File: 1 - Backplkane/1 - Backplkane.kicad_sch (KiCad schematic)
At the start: 37 parts, among them J1 BUS 1, J10 EXTENDED BUS, J11 5V DC, J2 BUS 2, J3 BUS 3, J4 BUS 4, J5 BUS 5, J6 BUS 6, J7 BUS 7, J8 BUS 8, J9 BASIC BUS, U1 LD1117AV33

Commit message: Converted files from version 6 to 7 of KiCad
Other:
- company: Frederic Segard - aka: The Micro Hobbyist -> Frederic Segard
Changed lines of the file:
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@@
   (title_block
     (title "8-slot ISA-style backblane with breadboard connectivity")
-    (date "2022-10-12")
-    (rev "1.5")
-    (company "Frederic Segard - aka: The Micro Hobbyist")
+    (date "2023-08-22")
+    (rev "1.1")
+    (company "Frederic Segard")
+    (comment 1 "@microhobbyist")
   )
   (junction (at 180.34 152.4) (diameter 0) (color 0 0 0 0)
@@
     )
   )
-  (symbol (lib_id "Graphic:Logo_Open_Hardware_Small") (at 258.445 180.34 0) (unit 1)
-    (in_bom no) (on_board no) (dnp no) (fields_autoplaced)
-    (property "Reference" "#LOGO1" (at 258.445 173.355 0)
+  (symbol (lib_id "Graphic:Logo_Open_Hardware_Small") (at 259.08 180.34 0) (unit 1)
+    (in_bom no) (on_board yes) (dnp no) (fields_autoplaced)
+    (property "Reference" "#LOGO1" (at 259.08 173.355 0)
       (effects (font (size 1.27 1.27)) hide)
     )
-    (property "Value" "Logo_Open_Hardware_Small" (at 258.445 186.055 0)
+    (property "Value" "Logo_Open_Hardware_Small" (at 259.08 186.055 0)
       (effects (font (size 1.27 1.27)) hide)
     )
-    (property "Footprint" "Symbol:OSHW-Logo2_9.8x8mm_SilkScreen" (at 258.445 180.34 0)
+    (property "Footprint" "Symbol:OSHW-Logo2_9.8x8mm_SilkScreen" (at 259.08 180.34 0)
       (effects (font (size 1.27 1.27)) hide)
     )
-    (property "Datasheet" "~" (at 258.445 180.34 0)
+    (property "Datasheet" "~" (at 259.08 180.34 0)
       (effects (font (size 1.27 1.27)) hide)
     )
-    (property "Sim.Enable" "0" (at 258.445 180.34 0)
+    (property "Sim.Enable" "0" (at 259.08 180.34 0)
       (effects (font (size 1.27 1.27)) hide)
     )

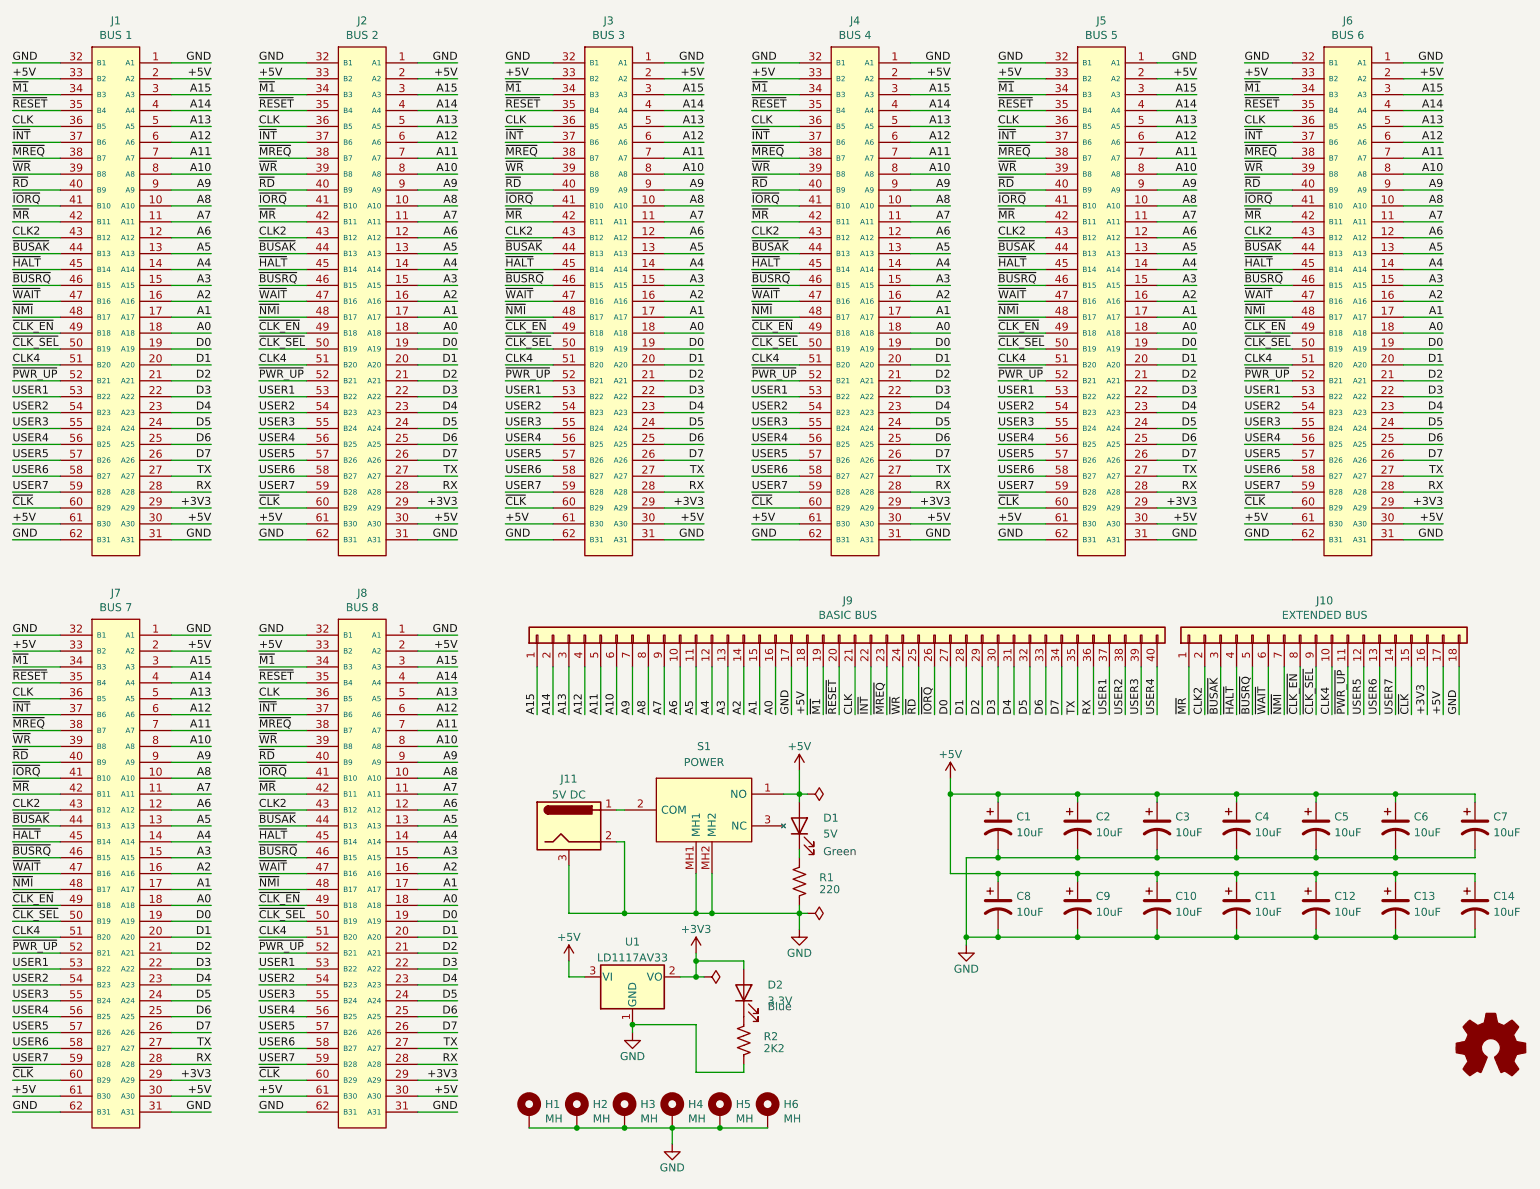
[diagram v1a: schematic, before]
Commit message: Added serial card, still needs work
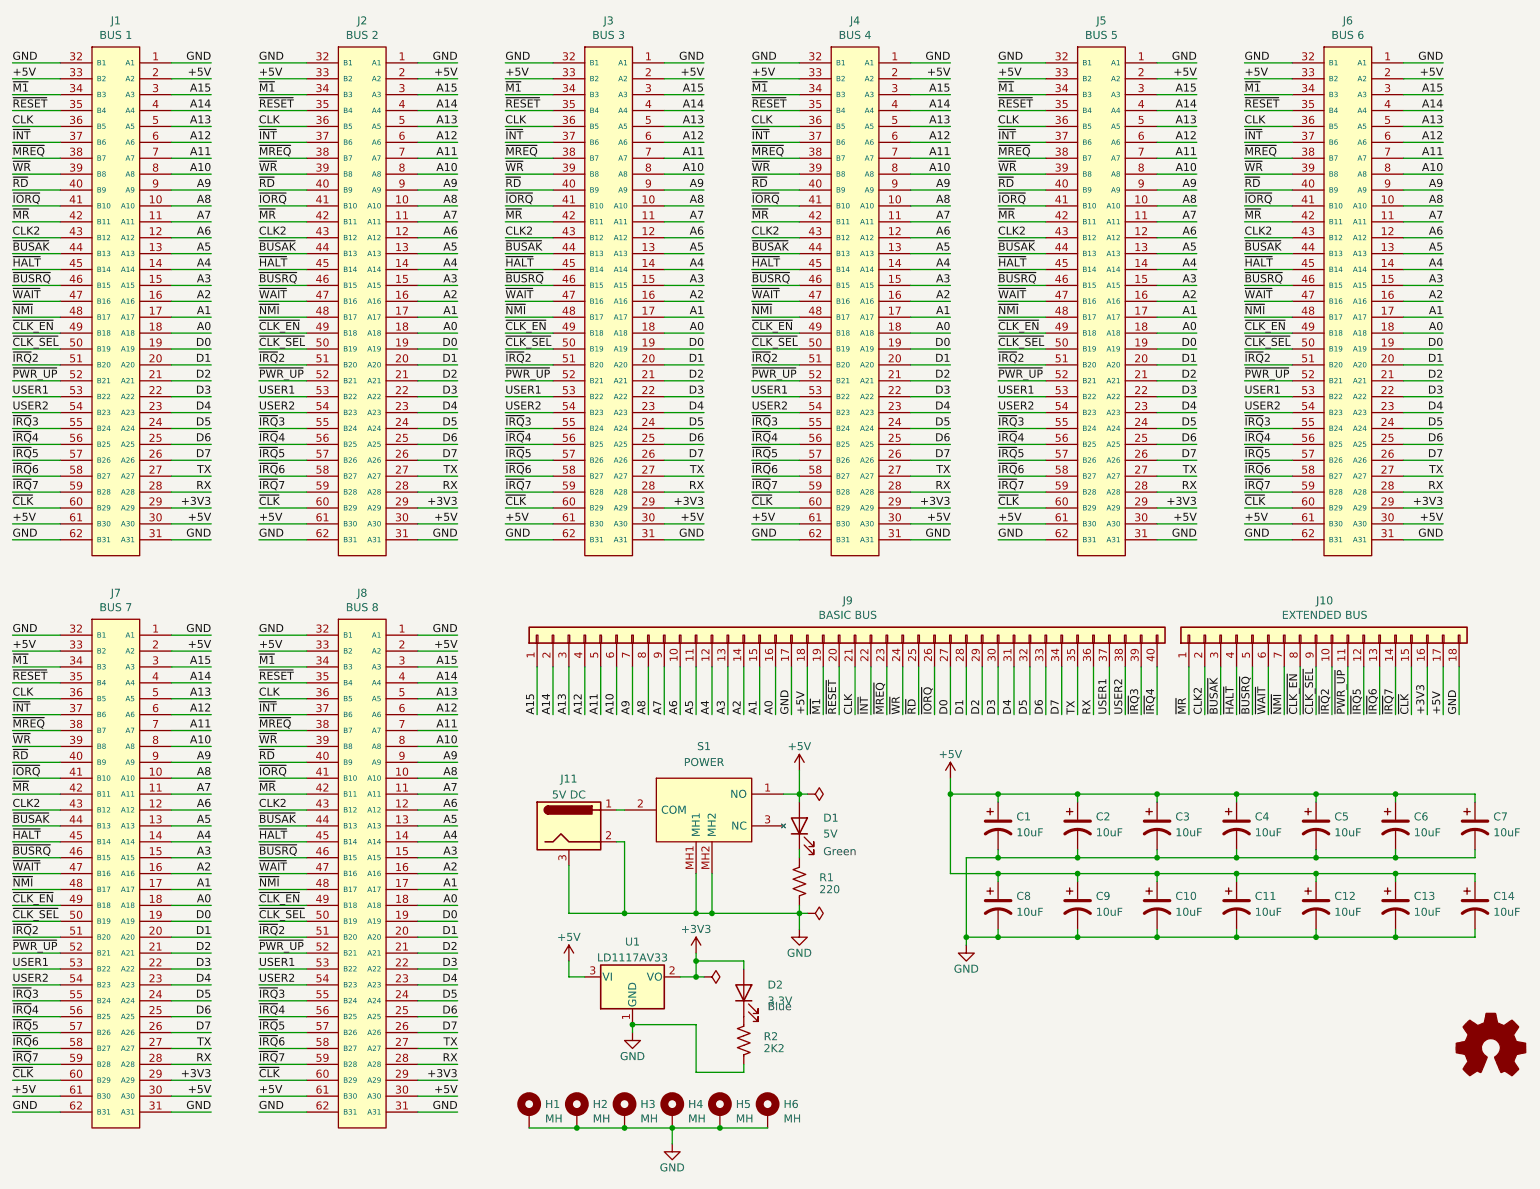
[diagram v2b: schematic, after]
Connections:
- net CLK4 renamed ~{IRQ}2
- net USER3 renamed ~{IRQ}3
- net USER4 renamed ~{IRQ}4
- net USER5 renamed ~{IRQ}5
- net USER6 renamed ~{IRQ}6
- net USER7 renamed ~{IRQ}7
